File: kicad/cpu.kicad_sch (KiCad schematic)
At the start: 24 parts, among them U1 W65C816S, U2 74AC04, U3 74AC245, U4 74AC573, U5 DS1813-5+, X1 MXO45HS

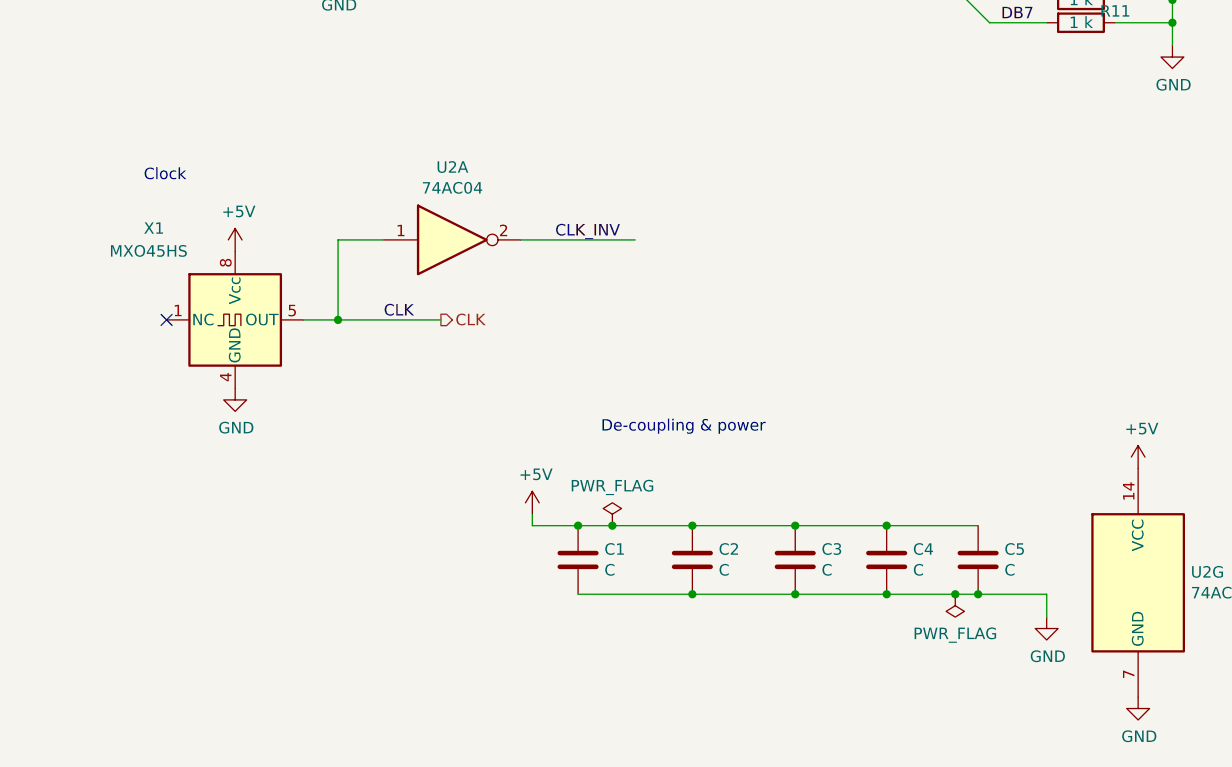
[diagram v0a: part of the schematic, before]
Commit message: update computer, move test program to use native mode
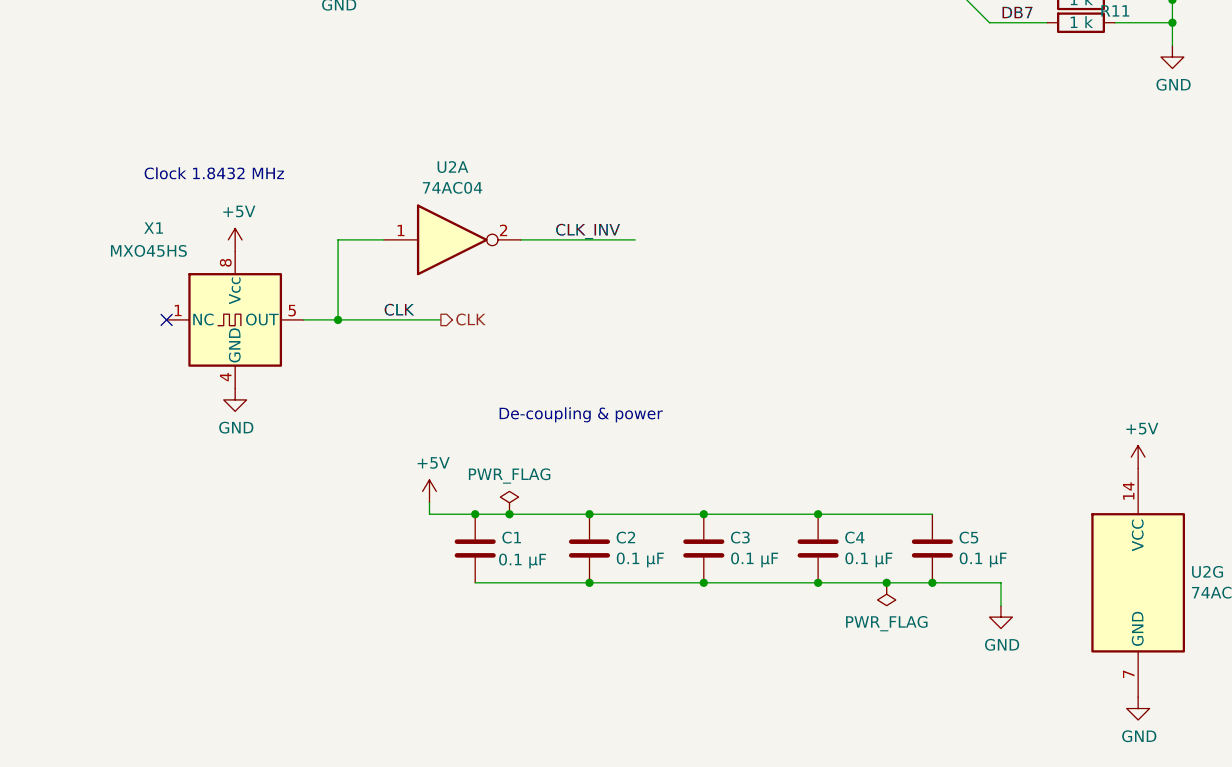
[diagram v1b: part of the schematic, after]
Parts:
- C1, C2, C3, C4, C5: value C -> 0.1 µF
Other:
- note added: "Clock 1.8432 MHz"
- note removed: "Clock"
- moved on the sheet: C1, C2, C3, C4, C5

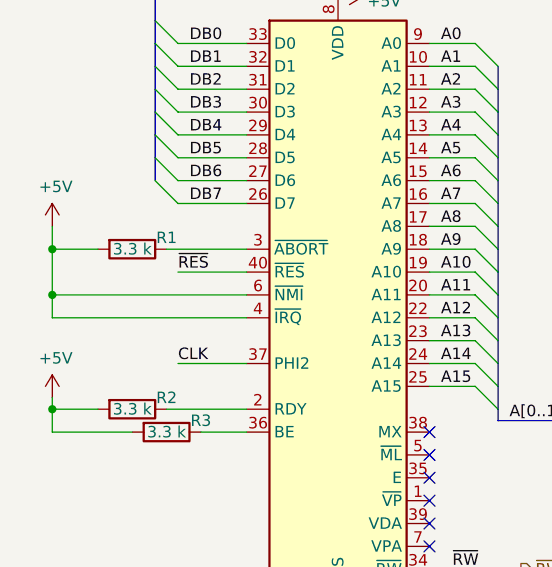
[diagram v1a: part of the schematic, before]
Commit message: connect IRQ output of 65C22 to CPU NMI
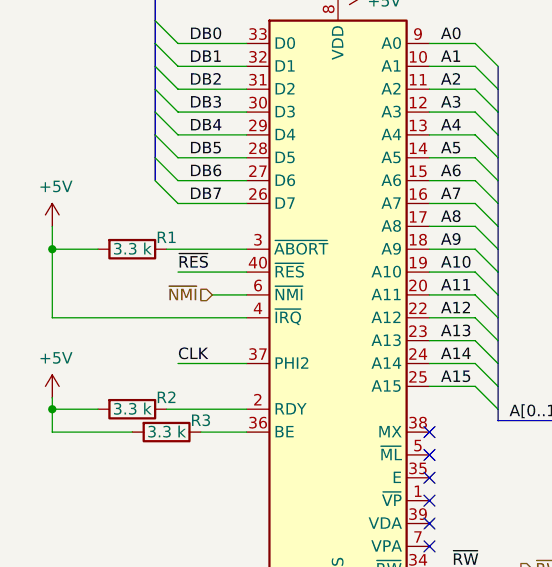
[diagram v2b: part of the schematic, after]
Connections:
- net +5V: no longer U1.6 (~{NMI})
- new net ~{NMI}: U1.6 (~{NMI})
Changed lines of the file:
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@@
   (junction (at 154.94 96.52) (diameter 0) (color 0 0 0 0)
-  )
-  (junction (at 30.48 69.85) (diameter 0) (color 0 0 0 0)
   )
   (junction (at 154.94 111.76) (diameter 0) (color 0 0 0 0)
@@
     (stroke (width 0) (type default) (color 0 0 0 0))
   )
-  (wire (pts (xy 30.48 72.39) (xy 30.48 69.85))
-    (stroke (width 0) (type default) (color 0 0 0 0))
-  )
   (wire (pts (xy 82.55 135.89) (xy 95.25 135.89))
     (stroke (width 0) (type default) (color 0 0 0 0))
@@
     (stroke (width 0) (type default) (color 0 0 0 0))
   )
-  (wire (pts (xy 30.48 69.85) (xy 52.07 69.85))
-    (stroke (width 0) (type default) (color 0 0 0 0))
-  )
   (wire (pts (xy 44.45 52.07) (xy 52.07 52.07))
     (stroke (width 0) (type default) (color 0 0 0 0))
@@
     (stroke (width 0) (type default) (color 0 0 0 0))
   )
+  (wire (pts (xy 48.26 69.85) (xy 52.07 69.85))
+    (stroke (width 0) (type default) (color 0 0 0 0))
+  )
   (wire (pts (xy 62.23 144.78) (xy 62.23 135.89))
     (stroke (width 0) (type default) (color 0 0 0 0))
@@
     (stroke (width 0) (type default) (color 0 0 0 0))
   )
-  (wire (pts (xy 30.48 64.77) (xy 30.48 69.85))
+  (wire (pts (xy 30.48 64.77) (xy 30.48 72.39))
     (stroke (width 0) (type default) (color 0 0 0 0))
   )
@@
     (effects (font (size 1.27 1.27)) (justify left bottom))
   )
+  (hierarchical_label "~{NMI}" (shape input) (at 48.26 69.85 180)
+    (effects (font (size 1.27 1.27)) (justify right))
+  )
   (hierarchical_label "~{RES}" (shape output) (at 236.22 133.35 0)
